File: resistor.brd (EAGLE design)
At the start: 50.8 x 17.8 mm, 2 parts

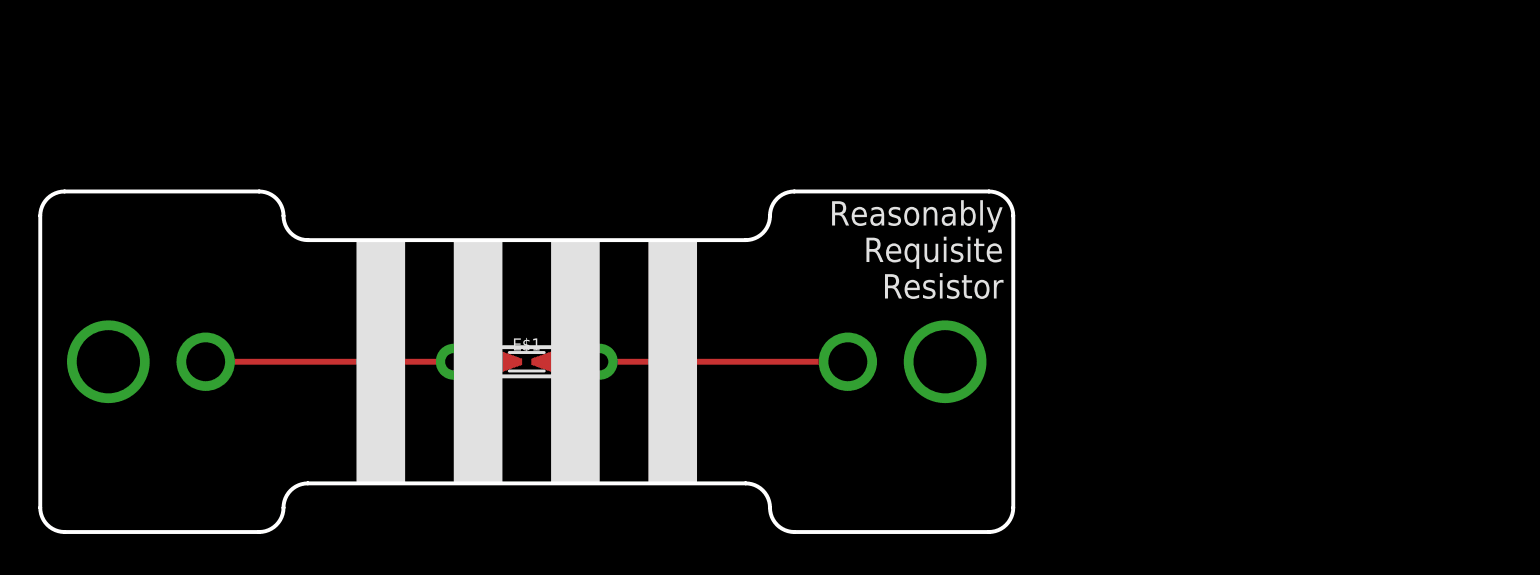
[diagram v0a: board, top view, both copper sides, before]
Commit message: embiggened resitor
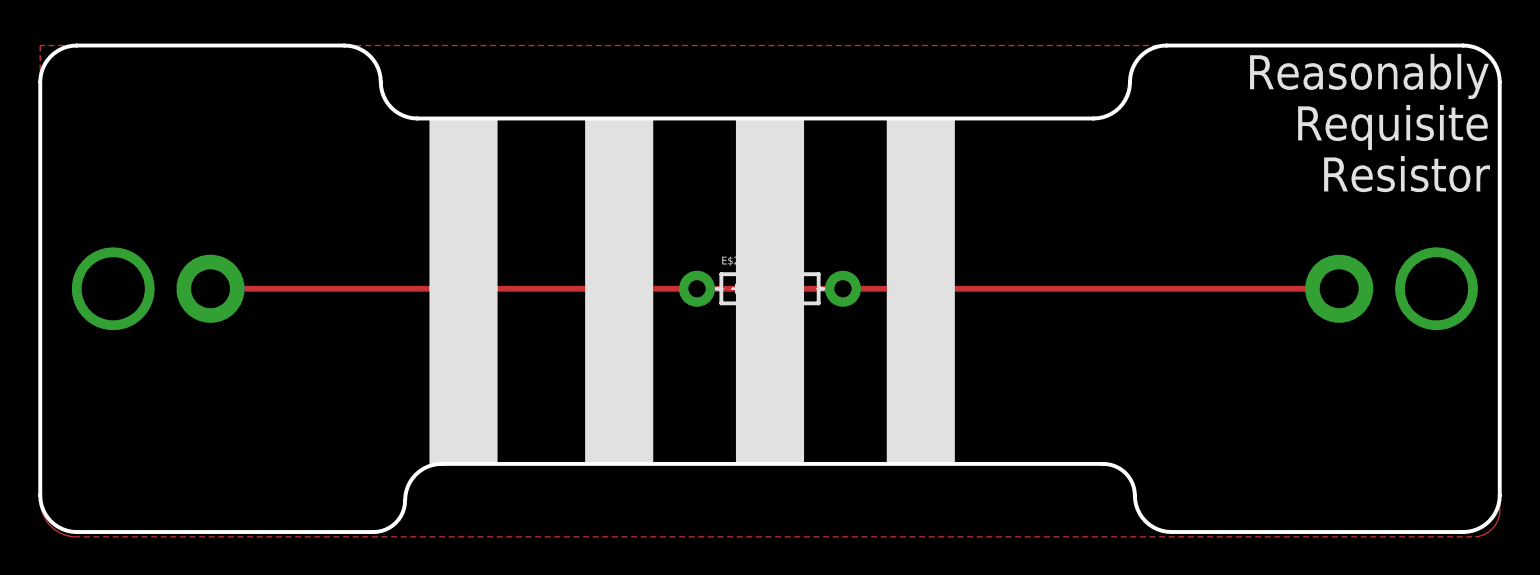
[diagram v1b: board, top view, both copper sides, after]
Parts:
- moved E$1 13.3 mm to (38.1, 12.7)
- moved E$2 13.3 mm to (38.1, 12.7)
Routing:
- net S$4: track 15.7 -> 28.7 mm
- net S$3: track 15.9 -> 28.3 mm
- added copper zone on layer 1, net S$5
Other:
- board size 50.8 x 17.8 mm -> 76.2 x 25.4 mm
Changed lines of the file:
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@@
 <board>
 <plain>
-<wire x1="0" y1="16.51" x2="0" y2="1.27" width="0.2032" layer="20"/>
-<wire x1="0" y1="1.27" x2="1.27" y2="0" width="0.2032" layer="20" curve="90"/>
-<wire x1="1.27" y1="0" x2="11.43" y2="0" width="0.2032" layer="20"/>
-<wire x1="11.43" y1="0" x2="12.7" y2="1.27" width="0.2032" layer="20" curve="90"/>
-<wire x1="12.7" y1="1.27" x2="13.97" y2="2.54" width="0.2032" layer="20" curve="-90"/>
-<wire x1="13.97" y1="2.54" x2="36.83" y2="2.54" width="0.2032" layer="20"/>
-<wire x1="36.83" y1="2.54" x2="38.1" y2="1.27" width="0.2032" layer="20" curve="-90"/>
-<wire x1="38.1" y1="1.27" x2="39.37" y2="0" width="0.2032" layer="20" curve="90"/>
-<wire x1="39.37" y1="0" x2="49.53" y2="0" width="0.2032" layer="20"/>
-<wire x1="49.53" y1="0" x2="50.8" y2="1.27" width="0.2032" layer="20" curve="90"/>
-<wire x1="50.8" y1="1.27" x2="50.8" y2="16.51" width="0.2032" layer="20"/>
-<wire x1="50.8" y1="16.51" x2="49.53" y2="17.78" width="0.2032" layer="20" curve="90"/>
-<wire x1="49.53" y1="17.78" x2="39.37" y2="17.78" width="0.2032" layer="20"/>
-<wire x1="39.37" y1="17.78" x2="38.1" y2="16.51" width="0.2032" layer="20" curve="90"/>
-<wire x1="38.1" y1="16.51" x2="36.83" y2="15.24" width="0.2032" layer="20" curve="-90"/>
-<wire x1="36.83" y1="15.24" x2="13.97" y2="15.24" width="0.2032" layer="20"/>
-<wire x1="13.97" y1="15.24" x2="12.7" y2="16.51" width="0.2032" layer="20" curve="-90"/>
-<wire x1="12.7" y1="16.51" x2="11.43" y2="17.78" width="0.2032" layer="20" curve="90"/>
-<wire x1="11.43" y1="17.78" x2="1.27" y2="17.78" width="0.2032" layer="20"/>
-<wire x1="1.27" y1="17.78" x2="0" y2="16.51" width="0.2032" layer="20" curve="90"/>
-<rectangle x1="16.51" y1="2.54" x2="19.05" y2="15.24" layer="21"/>
-<rectangle x1="21.59" y1="2.54" x2="24.13" y2="15.24" layer="21"/>
-<rectangle x1="26.67" y1="2.54" x2="29.21" y2="15.24" layer="21"/>
-<rectangle x1="31.75" y1="2.54" x2="34.29" y2="15.24" layer="22" rot="R180"/>
-<rectangle x1="26.67" y1="2.54" x2="29.21" y2="15.24" layer="22" rot="R180"/>
-<rectangle x1="21.59" y1="2.54" x2="24.13" y2="15.24" layer="22" rot="R180"/>
-<rectangle x1="16.51" y1="2.54" x2="19.05" y2="15.24" layer="22"/>
-<rectangle x1="31.75" y1="2.54" x2="34.29" y2="15.24" layer="21"/>
-<text x="50.292" y="17.272" size="1.27" layer="21" font="vector" ratio="15" align="top-right">Reasonably
+<wire x1="55.499" y1="3.556" x2="20.955" y2="3.556" width="0.2032" layer="20"/>
+<wire x1="20.955" y1="3.556" x2="19.05" y2="1.651" width="0.2032" layer="20" curve="90"/>
+<wire x1="0" y1="23.495" x2="0" y2="1.905" width="0.2032" layer="20"/>
+<wire x1="0" y1="1.905" x2="1.905" y2="0" width="0.2032" layer="20" curve="90"/>
+<wire x1="1.905" y1="0" x2="17.399" y2="0" width="0.2032" layer="20"/>
+<wire x1="17.399" y1="0" x2="19.05" y2="1.651" width="0.2032" layer="20" curve="90"/>
+<wire x1="55.499" y1="3.556" x2="57.15" y2="1.905" width="0.2032" layer="20" curve="-90"/>
+<wire x1="57.15" y1="1.905" x2="59.055" y2="0" width="0.2032" layer="20" curve="90"/>
+<wire x1="59.055" y1="0" x2="74.295" y2="0" width="0.2032" layer="20"/>
+<wire x1="74.295" y1="0" x2="76.2" y2="1.905" width="0.2032" layer="20" curve="90"/>
+<wire x1="76.2" y1="1.905" x2="76.2" y2="23.495" width="0.2032" layer="20"/>
+<wire x1="76.2" y1="23.495" x2="74.295" y2="25.4" width="0.2032" layer="20" curve="90"/>
+<wire x1="74.295" y1="25.4" x2="58.801" y2="25.4" width="0.2032" layer="20"/>
+<wire x1="58.801" y1="25.4" x2="56.896" y2="23.495" width="0.2032" layer="20" curve="90"/>
+<wire x1="56.896" y1="23.495" x2="54.991" y2="21.59" width="0.2032" layer="20" curve="-90"/>
+<wire x1="54.991" y1="21.59" x2="19.685" y2="21.59" width="0.2032" layer="20"/>
+<wire x1="19.685" y1="21.59" x2="17.78" y2="23.495" width="0.2032" layer="20" curve="-90"/>
+<wire x1="17.78" y1="23.495" x2="15.875" y2="25.4" width="0.2032" layer="20" curve="90"/>
+<wire x1="15.875" y1="25.4" x2="1.905" y2="25.4" width="0.2032" layer="20"/>
+<wire x1="1.905" y1="25.4" x2="0" y2="23.495" width="0.2032" layer="20" curve="90"/>
+<rectangle x1="20.32" y1="3.556" x2="23.876" y2="21.59" layer="21"/>
+<rectangle x1="20.32" y1="3.556" x2="23.876" y2="21.59" layer="22"/>
+<text x="75.692" y="24.892" size="1.778" layer="21" font="vector" ratio="15" align="top-right">Reasonably
 Requisite
 Resistor</text>
-<text x="50.292" y="17.018" size="0.889" layer="22" font="vector" ratio="15" distance="25" rot="MR0" align="top-left">I let electricity
+<text x="75.692" y="24.638" size="1.27" layer="22" font="vector" ratio="15" distance="25" rot="MR0" align="top-left">I let electricity
 pass, but not too
 fast! You can use me
 to add small voltage
 to input signals, </text>
-<text x="50.292" y="6.604" size="1.016" layer="22" font="vector" ratio="15" distance="25" rot="MR0" align="top-left">restrict current to
+<text x="75.692" y="8.128" size="1.27" layer="22" font="vector" ratio="15" distance="25" rot="MR0" align="top-left">restrict current to
 switches or lights,
 or simply generate
  heat!</text>
-<polygon width="0.2032" layer="22">
-<vertex x="12.954" y="10.922" curve="90"/>
-<vertex x="14.224" y="12.192"/>
-<vertex x="14.224" y="12.954" curve="90"/>
-<vertex x="12.954" y="14.224"/>
-<vertex x="5.334" y="14.224" curve="90"/>
-<vertex x="4.064" y="12.954"/>
-<vertex x="4.064" y="12.192" curve="90"/>
-<vertex x="5.334" y="10.922"/>
-</polygon>
-<text x="0.254" y="16.764" size="1.016" layer="22" font="vector" ratio="15" distance="25" rot="MR0" align="top-right">This is my
+<text x="0.254" y="24.384" size="1.27" layer="22" font="vector" ratio="15" distance="25" rot="MR0" align="top-right">This is my
 resistance value!
 </text>
-<text x="0.254" y="6.35" size="1.016" layer="22" font="vector" ratio="15" distance="25" rot="MR0" align="top-right">If you know the
+<text x="0.508" y="8.128" size="1.27" layer="22" font="vector" ratio="15" distance="25" rot="MR0" align="top-right">If you know the
 trick, you can
 read this from my
 colored bands!</text>
-<text x="3.81" y="13.208" size="1.016" layer="22" font="vector" ratio="15" distance="25" rot="MR0" align="top-left">ohms</text>
+<text x="4.826" y="19.05" size="1.27" layer="22" font="vector" ratio="15" distance="25" rot="MR0" align="top-left">ohms</text>
+<polygon width="0.2032" layer="22">
+<vertex x="15.24" y="19.558" curve="90"/>
+<vertex x="13.716" y="21.082"/>
+<vertex x="7.366" y="21.082" curve="90"/>
+<vertex x="5.588" y="19.304" curve="90"/>
+<vertex x="7.112" y="17.78"/>
+<vertex x="13.462" y="17.78" curve="90"/>
+</polygon>
+<rectangle x1="36.322" y1="3.556" x2="39.878" y2="21.59" layer="21"/>
+<rectangle x1="28.448" y1="3.556" x2="32.004" y2="21.59" layer="21"/>
+<rectangle x1="28.448" y1="3.556" x2="32.004" y2="21.59" layer="22"/>
+<rectangle x1="36.322" y1="3.556" x2="39.878" y2="21.59" layer="22"/>
+<rectangle x1="44.196" y1="3.556" x2="47.752" y2="21.59" layer="21"/>
+<rectangle x1="44.196" y1="3.556" x2="47.752" y2="21.59" layer="22"/>
 </plain>
 <attributes>
@@
 </class>
 </classes>
-<designrules name="default">
+<designrules name="default *">
 <description language="en">&lt;b&gt;EAGLE Design Rules&lt;/b&gt;
 &lt;p&gt;
@@
 <param name="mdViaViaSameLayer" value="8mil"/>
 <param name="mnLayersViaInSmd" value="2"/>
-<param name="mdCopperDimension" value="40mil"/>
+<param name="mdCopperDimension" value="15mil"/>
 <param name="mdDrill" value="8mil"/>
 <param name="mdSmdStop" value="0mil"/>
@@
 </autorouter>
 <elements>
-<element name="E$1" library="tekdemo" package="0402-0603-0805-UNIVERSAL" value="" x="25.4" y="8.89"/>
-<element name="E$2" library="tekdemo" package="AXIAL-0.3" value="" x="25.4" y="8.89"/>
+<element name="E$1" library="tekdemo" package="0402-0603-0805-UNIVERSAL" value="" x="38.1" y="12.7"/>
+<element name="E$2" library="tekdemo" package="AXIAL-0.3" value="" x="38.1" y="12.7"/>
 </elements>
 <signals>
 <signal name="S$1">
-<via x="3.556" y="8.89" extent="1-16" drill="3.302"/>
+<via x="3.81" y="12.7" extent="1-16" drill="3.302"/>
 </signal>
 <signal name="S$2">
-<via x="47.244" y="8.89" extent="1-16" drill="3.302"/>
+<via x="72.898" y="12.7" extent="1-16" drill="3.302"/>
 </signal>
 <signal name="S$3">
-<via x="8.636" y="8.89" extent="1-16" drill="2.032"/>
-<wire x1="8.636" y1="8.89" x2="24.511" y2="8.89" width="0.3048" layer="1"/>
+<via x="8.89" y="12.7" extent="1-16" drill="2.032" diameter="3.556"/>
+<wire x1="8.89" y1="12.7" x2="37.211" y2="12.7" width="0.3048" layer="1"/>
 </signal>
 <signal name="S$4">
-<via x="42.164" y="8.89" extent="1-16" drill="2.032"/>
-<wire x1="42.164" y1="8.89" x2="26.416" y2="8.89" width="0.3048" layer="1"/>
+<via x="67.818" y="12.7" extent="1-16" drill="2.032" diameter="3.556"/>
+<wire x1="67.818" y1="12.7" x2="39.116" y2="12.7" width="0.3048" layer="1"/>
+</signal>
+<signal name="S$5">
+<polygon width="0.381" layer="1" isolate="0.381">
+<vertex x="0" y="25.4"/>
+<vertex x="0" y="1.778" curve="90"/>
+<vertex x="1.778" y="-0.254"/>
+<vertex x="74.93" y="-0.254" curve="90"/>
+<vertex x="76.2" y="1.27"/>
+<vertex x="76.2" y="23.622" curve="90"/>
+<vertex x="74.422" y="25.4"/>
+</polygon>
 </signal>
 </signals>
